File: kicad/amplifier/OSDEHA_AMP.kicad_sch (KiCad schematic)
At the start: 62 parts, among them J1 INPUT, J2 HEATERS DC, J3 PSU HV, J4 OUTPUT, J5 DHT FIL2, J6 DHT FIL1, Q1 DN2540N5-G, Q2 DN2540N5-G, Q3 STF3LN80K5, Q4 STF3LN80K5, SW1 SW_DPDT_x2, U1 6E5P, U2 6E5P, U3 801A, U4 801A

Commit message: amp pcb
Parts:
- R15, R20: footprint Resistor_THT:R_Axial_DIN0207_L6.3mm_D2.5mm_P10.16mm_Horizontal -> Resistor_THT:R_Axial_DIN0207_L6.3mm_D2.5mm_P2.54mm_Vertical
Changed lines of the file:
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@@
       (effects (font (size 1.27 1.27)))
     )
-    (property "Footprint" "Resistor_THT:R_Axial_DIN0207_L6.3mm_D2.5mm_P10.16mm_Horizontal" (at 193.548 173.99 90)
+    (property "Footprint" "Resistor_THT:R_Axial_DIN0207_L6.3mm_D2.5mm_P2.54mm_Vertical" (at 193.548 173.99 90)
       (effects (font (size 1.27 1.27)) hide)
     )
@@
       (effects (font (size 1.27 1.27)))
     )
-    (property "Footprint" "Resistor_THT:R_Axial_DIN0207_L6.3mm_D2.5mm_P10.16mm_Horizontal" (at 166.878 173.99 90)
-      (effects (font (size 1.27 1.27)) hide)
-    )
+    (property "Footprint" "Resistor_THT:R_Axial_DIN0207_L6.3mm_D2.5mm_P2.54mm_Vertical" (at 166.878 173.99 90)
+      (effects (font (size 1.27 1.27)) hide)
+    )

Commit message: up
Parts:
- removed D1, D2: 15V, Diode_THT:D_DO-41_SOD81_P7.62mm_Horizontal, symbol Device:D_Zener
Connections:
- net at R10.1, R6.2: now also R5.2; no longer R5.1
- net at Q1.1 (G): now also R5.1; no longer R5.2
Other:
- moved on the sheet: R5
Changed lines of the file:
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@@
   (junction (at 77.47 132.08) (diameter 0) (color 0 0 0 0)
   )
-  (junction (at 100.33 167.64) (diameter 0) (color 0 0 0 0)
-  )
   (junction (at 213.36 185.42) (diameter 0) (color 0 0 0 0)
   )
@@
     (stroke (width 0) (type default))
   )
-  (wire (pts (xy 100.33 177.8) (xy 100.33 179.07))
+  (wire (pts (xy 100.33 162.56) (xy 100.33 179.07))
     (stroke (width 0) (type default))
   )
@@
     (stroke (width 0) (type default))
   )
-  (wire (pts (xy 100.33 162.56) (xy 100.33 167.64))
-    (stroke (width 0) (type default))
-  )
   (wire (pts (xy 198.12 162.56) (xy 198.12 161.29))
     (stroke (width 0) (type default))
@@
     (stroke (width 0) (type default))
   )
-  (wire (pts (xy 100.33 167.64) (xy 100.33 170.18))
-    (stroke (width 0) (type default))
-  )
   (wire (pts (xy 151.13 185.42) (xy 157.48 185.42))
     (stroke (width 0) (type default))
@@
   )
   (wire (pts (xy 240.03 138.43) (xy 240.03 135.89))
-    (stroke (width 0) (type default))
-  )
-  (wire (pts (xy 100.33 162.56) (xy 107.95 162.56))
     (stroke (width 0) (type default))
   )
@@
     )
   )
-  (symbol (lib_id "Device:D_Zener") (at 104.14 167.64 0) (unit 1)
-    (in_bom yes) (on_board yes) (dnp no)
-    (property "Reference" "D1" (at 101.6 170.18 0)
-      (effects (font (size 1.27 1.27)))
-    )
-    (property "Value" "15V" (at 105.41 170.18 0)
-      (effects (font (size 1.27 1.27)))
-    )
-    (property "Footprint" "Diode_THT:D_DO-41_SOD81_P7.62mm_Horizontal" (at 104.14 167.64 0)
-      (effects (font (size 1.27 1.27)) hide)
-    )
-    (property "Datasheet" "https://diotec.com/request/datasheet/zy1.pdf" (at 104.14 167.64 0)
-      (effects (font (size 1.27 1.27)) hide)
-    )
-    (property "MPN" "ZY15" (at 104.14 167.64 0)
-      (effects (font (size 1.27 1.27)) hide)
-    )
-    (pin "2")
-    (pin "1")
-    (instances
-      (project "OSDEHA_AMP"
-        (path "/59cc4414-299b-49db-9f9a-b06f69a12073"
-          (reference "D1") (unit 1)
-        )
-      )
-    )
-  )
   (symbol (lib_id "Connector:Conn_01x02_Socket") (at 375.92 217.17 0) (unit 1)
     (in_bom yes) (on_board yes) (dnp no) (fields_autoplaced)
@@
     )
   )
-  (symbol (lib_id "Device:R") (at 100.33 173.99 180) (unit 1)
-    (in_bom yes) (on_board yes) (dnp no)
-    (property "Reference" "R5" (at 97.79 172.72 90)
-      (effects (font (size 1.27 1.27)) (justify left))
-    )
-    (property "Value" "300" (at 100.33 173.99 90)
-      (effects (font (size 1.27 1.27)))
-    )
-    (property "Footprint" "Resistor_THT:R_Axial_DIN0207_L6.3mm_D2.5mm_P10.16mm_Horizontal" (at 102.108 173.99 90)
-      (effects (font (size 1.27 1.27)) hide)
-    )
-    (property "Datasheet" "https://www.vishay.com/doc?31018" (at 100.33 173.99 0)
-      (effects (font (size 1.27 1.27)) hide)
-    )
-    (property "MPN" "CMF55300R00" (at 100.33 173.99 90)
+  (symbol (lib_id "Device:R") (at 104.14 162.56 270) (unit 1)
+    (in_bom yes) (on_board yes) (dnp no)
+    (property "Reference" "R5" (at 102.87 165.1 90)
+      (effects (font (size 1.27 1.27)) (justify left))
+    )
+    (property "Value" "300" (at 104.14 162.56 90)
+      (effects (font (size 1.27 1.27)))
+    )
+    (property "Footprint" "Resistor_THT:R_Axial_DIN0207_L6.3mm_D2.5mm_P10.16mm_Horizontal" (at 104.14 160.782 90)
+      (effects (font (size 1.27 1.27)) hide)
+    )
+    (property "Datasheet" "https://www.vishay.com/doc?31018" (at 104.14 162.56 0)
+      (effects (font (size 1.27 1.27)) hide)
+    )
+    (property "MPN" "CMF55300R00" (at 104.14 162.56 90)
       (effects (font (size 1.27 1.27)) hide)
     )
@@
         )
       )
-    )
-  )
-  (symbol (lib_id "Device:D_Zener") (at 111.76 167.64 0) (mirror y) (unit 1)
-    (in_bom yes) (on_board yes) (dnp no)
-    (property "Reference" "D2" (at 114.3 170.18 0)
-      (effects (font (size 1.27 1.27)))
-    )
-    (property "Value" "15V" (at 110.49 170.18 0)
-      (effects (font (size 1.27 1.27)))
-    )
-    (property "Footprint" "Diode_THT:D_DO-41_SOD81_P7.62mm_Horizontal" (at 111.76 167.64 0)
-      (effects (font (size 1.27 1.27)) hide)
-    )
-    (property "Datasheet" "https://diotec.com/request/datasheet/zy1.pdf" (at 111.76 167.64 0)
-      (effects (font (size 1.27 1.27)) hide)
-    )
-    (property "MPN" "ZY15" (at 111.76 167.64 0)
-      (effects (font (size 1.27 1.27)) hide)
-    )
-    (pin "2")
-    (pin "1")
-    (instances
-      (project "OSDEHA_AMP"
-        (path "/59cc4414-299b-49db-9f9a-b06f69a12073"
-          (reference "D2") (unit 1)
-        )
-      )

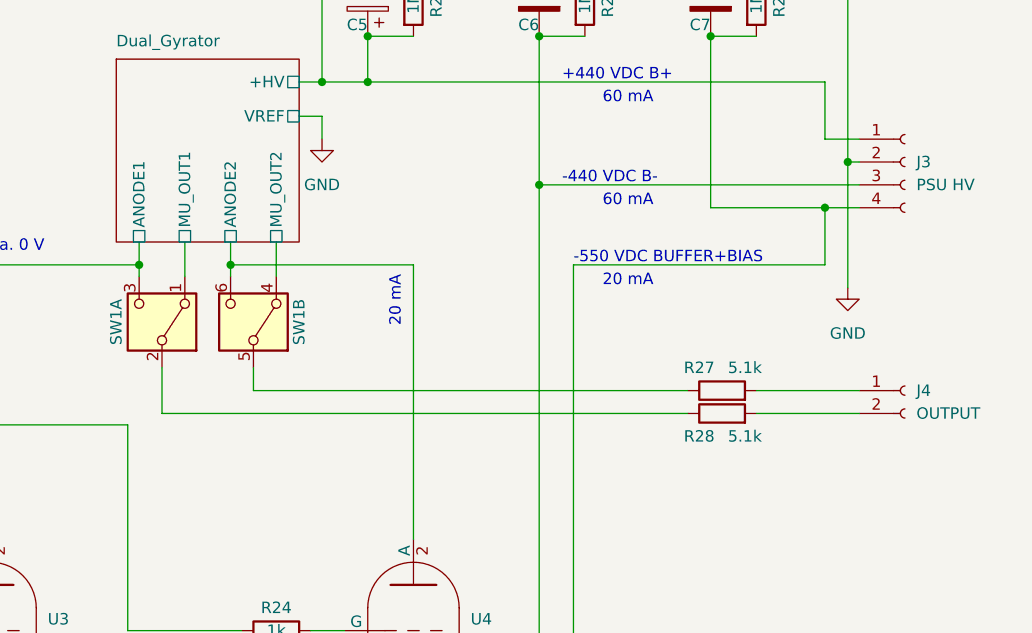
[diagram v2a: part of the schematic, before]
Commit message: safety resistors
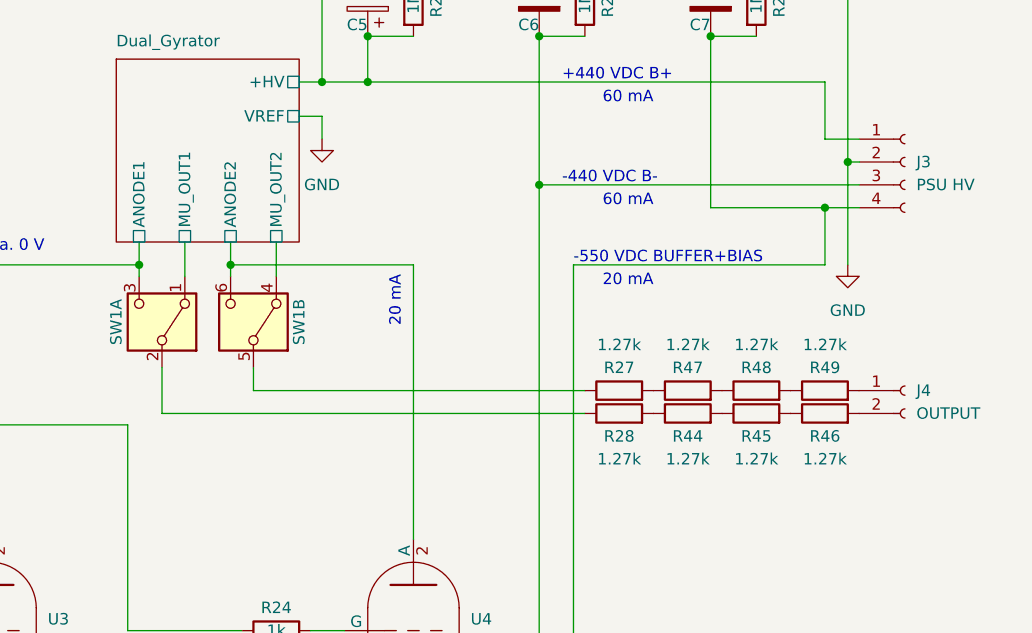
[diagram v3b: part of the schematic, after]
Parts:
- added R44, R45, R46, R47, R48, R49: 1.27k, Resistor_THT:R_Axial_DIN0207_L6.3mm_D2.5mm_P2.54mm_Vertical, symbol Device:R
- R27, R28: value 5.1k -> 1.27k; footprint Resistor_THT:R_Axial_DIN0207_L6.3mm_D2.5mm_P10.16mm_Horizontal -> Resistor_THT:R_Axial_DIN0207_L6.3mm_D2.5mm_P2.54mm_Vertical; MPN CMF555K1100 -> CMF551k2700
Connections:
- net at R27.2: now also R47.1; no longer J4.1 (Pin_1)
- net at R28.2: now also R44.1; no longer J4.2 (Pin_2)
- new net: R47.2, R48.1
- new net: R44.2, R45.1
- new net: R45.2, R46.1
- new net: R48.2, R49.1
- new net: J4.1 (Pin_1), R49.2
- new net: J4.2 (Pin_2), R46.2

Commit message: HV filter caps
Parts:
- removed C5, C6, C7: 51u, Capacitor_THT:CP_Radial_D25.0mm_P10.00mm_SnapIn, symbol Device:C_Polarized
- removed R25, R26, R29: 1M, Resistor_THT:R_Axial_DIN0207_L6.3mm_D2.5mm_P2.54mm_Vertical, symbol Device:R
- added C5, C6, C7: 220n 630 V, Capacitor_THT:C_Rect_L18.0mm_W9.0mm_P15.00mm_FKS3_FKP3, symbol Device:C
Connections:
- net Buffer_CCS_load1/NEG: now also C7.2
- net Dual_Gyrator/+HV: now also C5.2
- net GND: now also C5.1, C6.1, C7.1
- net at C1.2, C4.2, J3.3 (Pin_3)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: now also C6.2

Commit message: PCB rearrange
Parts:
- R15, R20: footprint Resistor_THT:R_Axial_DIN0207_L6.3mm_D2.5mm_P2.54mm_Vertical -> Resistor_THT:R_Axial_DIN0207_L6.3mm_D2.5mm_P10.16mm_Horizontal
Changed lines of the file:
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@@
       (effects (font (size 1.27 1.27)))
     )
-    (property "Footprint" "Resistor_THT:R_Axial_DIN0207_L6.3mm_D2.5mm_P2.54mm_Vertical" (at 193.548 173.99 90)
+    (property "Footprint" "Resistor_THT:R_Axial_DIN0207_L6.3mm_D2.5mm_P10.16mm_Horizontal" (at 193.548 173.99 90)
       (effects (font (size 1.27 1.27)) hide)
     )
@@
       (effects (font (size 1.27 1.27)))
     )
-    (property "Footprint" "Resistor_THT:R_Axial_DIN0207_L6.3mm_D2.5mm_P2.54mm_Vertical" (at 166.878 173.99 90)
-      (effects (font (size 1.27 1.27)) hide)
-    )
+    (property "Footprint" "Resistor_THT:R_Axial_DIN0207_L6.3mm_D2.5mm_P10.16mm_Horizontal" (at 166.878 173.99 90)
+      (effects (font (size 1.27 1.27)) hide)
+    )

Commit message: pcb
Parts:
- removed H5: VENTILATION, MountingHole:MountingHole_5mm, symbol Mechanical:MountingHole
- R23, R24: value 1k -> 100; MPN CMF551K0000 -> CMF55100R00

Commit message: pcb
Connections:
- net at Q2.2 (D), U1.9 (K), U2.9 (K): no longer U1.4 (K), U2.4 (K)
- no-connect marks 0 -> 2
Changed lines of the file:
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@@
     (title "OSDEHA Amplifier")
   )
-  (junction (at 99.06 140.97) (diameter 0) (color 0 0 0 0)
-  )
   (junction (at 187.96 120.65) (diameter 0) (color 0 0 0 0)
   )
@@
   (junction (at 213.36 185.42) (diameter 0) (color 0 0 0 0)
   )
-  (junction (at 132.08 140.97) (diameter 0) (color 0 0 0 0)
-  )
   (junction (at 161.29 161.29) (diameter 0) (color 0 0 0 0)
   )
@@
   (junction (at 224.79 143.51) (diameter 0) (color 0 0 0 0)
   )
+  (no_connect (at 93.98 139.7))
+  (no_connect (at 127 139.7))
   (wire (pts (xy 292.1 148.59) (xy 304.8 148.59))
     (stroke (width 0) (type default))
@@
     (stroke (width 0) (type default))
   )
-  (wire (pts (xy 99.06 139.7) (xy 99.06 140.97))
+  (wire (pts (xy 99.06 139.7) (xy 99.06 147.32))
     (stroke (width 0) (type default))
   )
@@
     (stroke (width 0) (type default))
   )
-  (wire (pts (xy 93.98 140.97) (xy 99.06 140.97))
-    (stroke (width 0) (type default))
-  )
   (wire (pts (xy 165.1 168.91) (xy 165.1 170.18))
     (stroke (width 0) (type default))
@@
     (stroke (width 0) (type default))
   )
-  (wire (pts (xy 127 139.7) (xy 127 140.97))
-    (stroke (width 0) (type default))
-  )
   (wire (pts (xy 369.57 93.98) (xy 369.57 87.63))
     (stroke (width 0) (type default))
@@
     (stroke (width 0) (type default))
   )
-  (wire (pts (xy 132.08 147.32) (xy 132.08 140.97))
-    (stroke (width 0) (type default))
-  )
   (wire (pts (xy 191.77 179.07) (xy 198.12 179.07))
     (stroke (width 0) (type default))
@@
     (stroke (width 0) (type default))
   )
-  (wire (pts (xy 93.98 139.7) (xy 93.98 140.97))
-    (stroke (width 0) (type default))
-  )
   (wire (pts (xy 313.69 87.63) (xy 318.77 87.63))
     (stroke (width 0) (type default))
@@
     (stroke (width 0) (type default))
   )
-  (wire (pts (xy 127 140.97) (xy 132.08 140.97))
-    (stroke (width 0) (type default))
-  )
   (wire (pts (xy 129.54 99.06) (xy 129.54 111.76))
     (stroke (width 0) (type default))
@@
     (stroke (width 0) (type default))
   )
-  (wire (pts (xy 99.06 140.97) (xy 99.06 147.32))
-    (stroke (width 0) (type default))
-  )
   (wire (pts (xy 137.16 128.27) (xy 137.16 119.38))
     (stroke (width 0) (type default))
@@
     (stroke (width 0) (type default))
   )
-  (wire (pts (xy 132.08 139.7) (xy 132.08 140.97))
-    (stroke (width 0) (type default))
-  )
+  (wire (pts (xy 132.08 139.7) (xy 132.08 147.32))
+    (stroke (width 0) (type default))
+  )
